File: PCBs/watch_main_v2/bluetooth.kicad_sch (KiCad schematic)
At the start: 24 parts, among them U301 NRF5340-QKAA-R7, Y301 32MHz

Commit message: Schematic v2 complete
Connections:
- net RST renamed SWD.RST
- net SWCLK renamed SWD.SWCLK
- net SWDIO renamed SWD.SWDIO
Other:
- moved on the sheet: C1922, L301, L302, L303, TP804, TP805, U301A, U301B, Y301

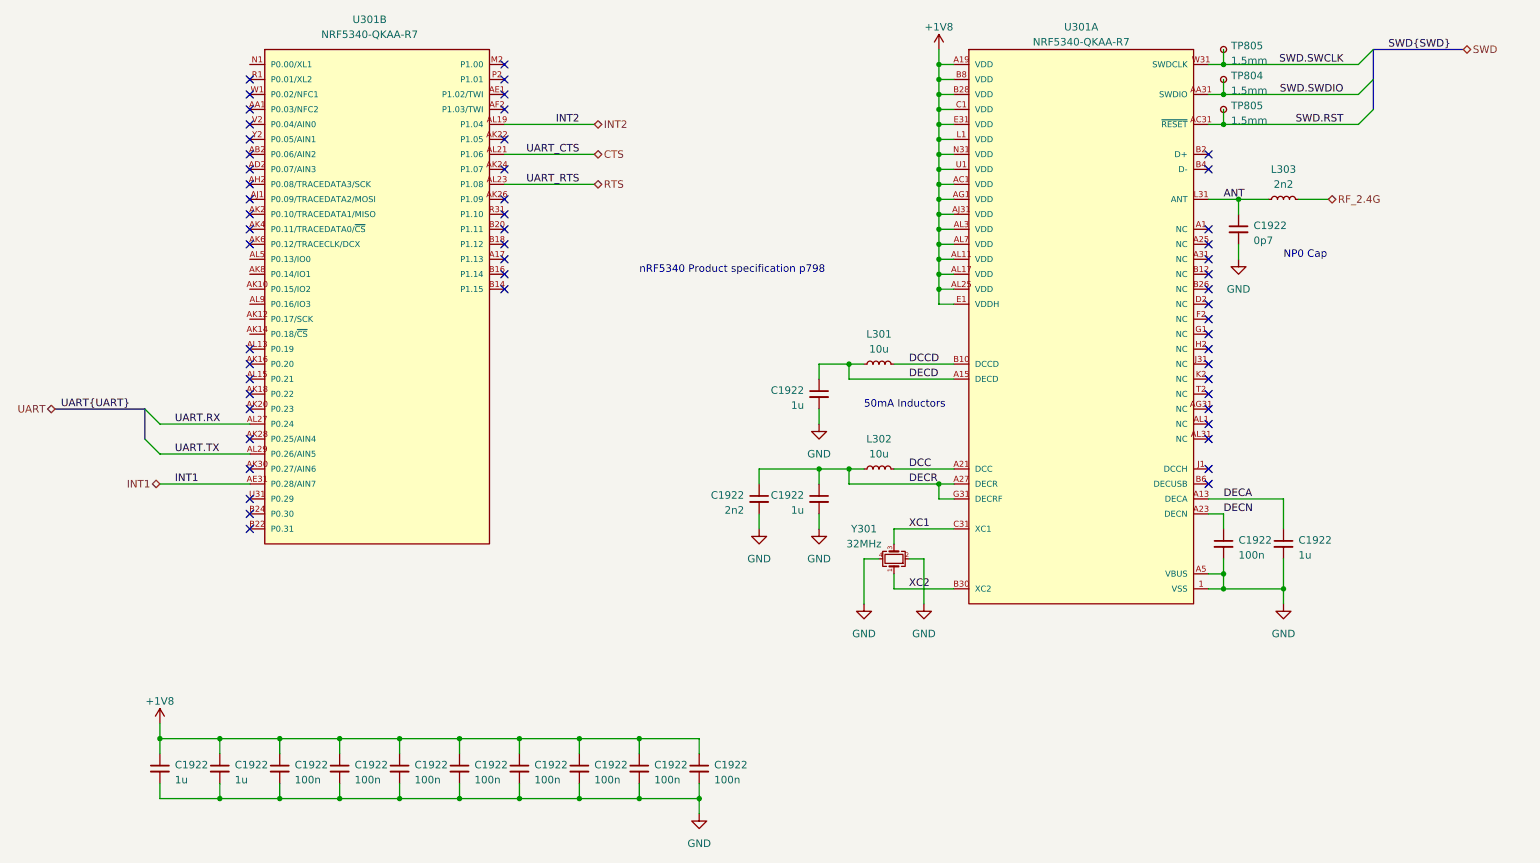
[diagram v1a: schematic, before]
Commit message: 262 Unrouted traces, fixed clearance issues
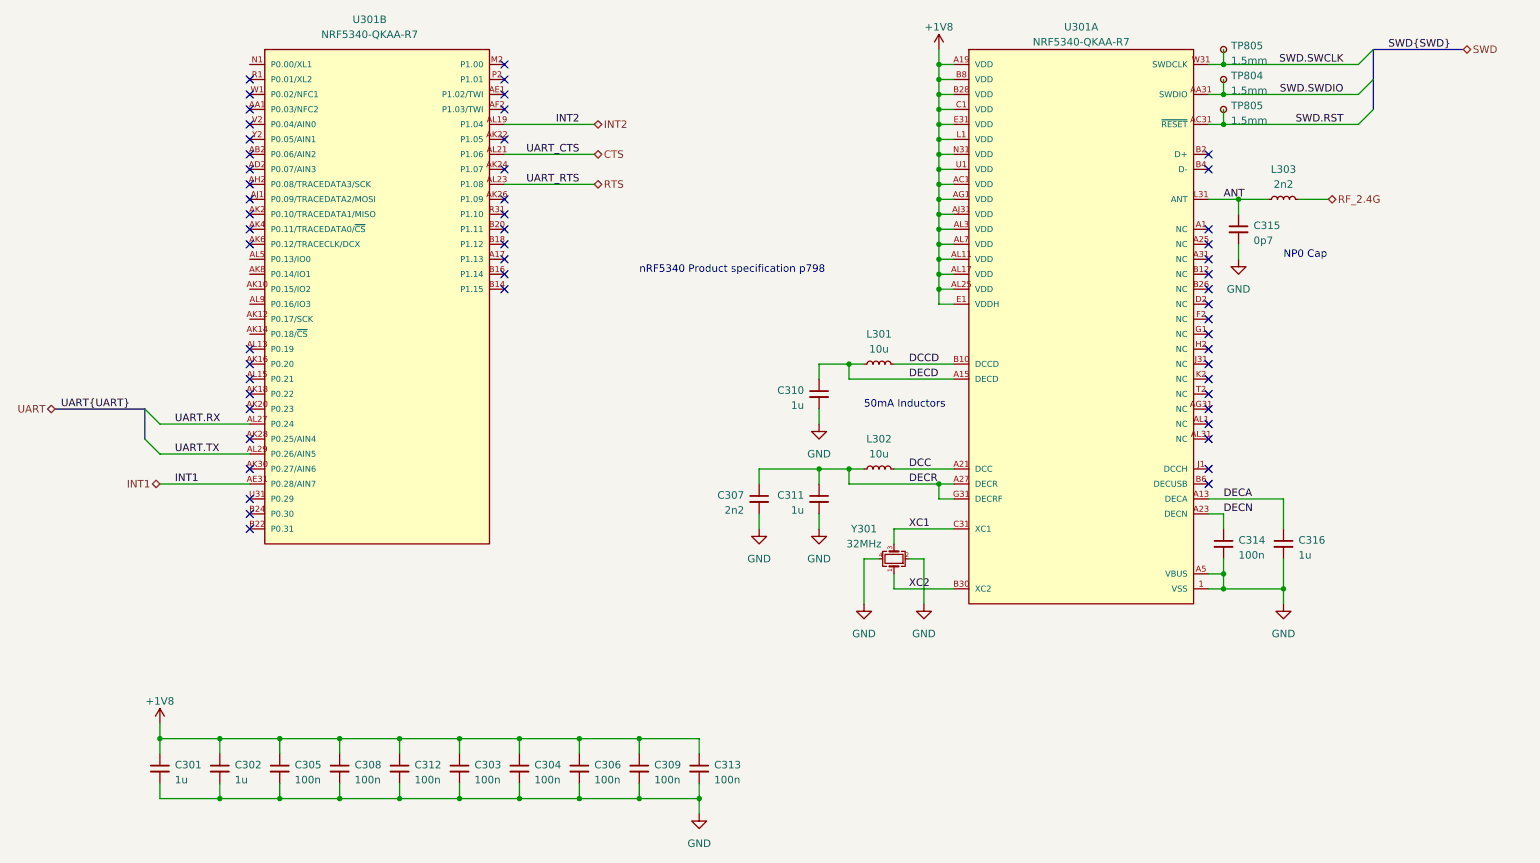
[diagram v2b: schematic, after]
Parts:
- renumbered C1922 to C301, C1922 to C302, C1922 to C303, C1922 to C304, C1922 to C305, C1922 to C306, C1922 to C307, C1922 to C308, C1922 to C309, C1922 to C310, C1922 to C311, C1922 to C312, C1922 to C313, C1922 to C314, C1922 to C315, C1922 to C316
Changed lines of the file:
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@@
   (symbol (lib_id "Device:C_Small") (at 228.6 73.66 0) (unit 1)
     (in_bom yes) (on_board yes) (dnp no)
-    (property "Reference" "C1922" (at 231.14 73.0313 0)
+    (property "Reference" "C315" (at 231.14 73.0313 0)
       (effects (font (size 1.27 1.27)) (justify left))
     )
@@
   (symbol (lib_id "Device:C_Small") (at 147.32 119.38 0) (mirror y) (unit 1)
     (in_bom yes) (on_board yes) (dnp no)
-    (property "Reference" "C1922" (at 144.78 118.7513 0)
+    (property "Reference" "C307" (at 144.78 118.7513 0)
       (effects (font (size 1.27 1.27)) (justify left))
     )
@@
   (symbol (lib_id "Device:C_Small") (at 127 165.1 0) (unit 1)
     (in_bom yes) (on_board yes) (dnp no)
-    (property "Reference" "C1922" (at 129.54 164.4713 0)
+    (property "Reference" "C309" (at 129.54 164.4713 0)
       (effects (font (size 1.27 1.27)) (justify left))
     )
@@
   (symbol (lib_id "Device:C_Small") (at 106.68 165.1 0) (unit 1)
     (in_bom yes) (on_board yes) (dnp no)
-    (property "Reference" "C1922" (at 109.22 164.4713 0)
+    (property "Reference" "C304" (at 109.22 164.4713 0)
       (effects (font (size 1.27 1.27)) (justify left))
     )
@@
   (symbol (lib_id "Device:C_Small") (at 45.72 165.1 0) (unit 1)
     (in_bom yes) (on_board yes) (dnp no)
-    (property "Reference" "C1922" (at 48.26 164.4713 0)
+    (property "Reference" "C301" (at 48.26 164.4713 0)
       (effects (font (size 1.27 1.27)) (justify left))
     )
@@
   (symbol (lib_id "Device:C_Small") (at 157.48 119.38 0) (mirror y) (unit 1)
     (in_bom yes) (on_board yes) (dnp no)
-    (property "Reference" "C1922" (at 154.94 118.7513 0)
+    (property "Reference" "C311" (at 154.94 118.7513 0)
       (effects (font (size 1.27 1.27)) (justify left))
     )
@@
   (symbol (lib_id "Device:C_Small") (at 116.84 165.1 0) (unit 1)
     (in_bom yes) (on_board yes) (dnp no)
-    (property "Reference" "C1922" (at 119.38 164.4713 0)
+    (property "Reference" "C306" (at 119.38 164.4713 0)
       (effects (font (size 1.27 1.27)) (justify left))
     )
@@
   (symbol (lib_id "Device:C_Small") (at 226.06 127 0) (unit 1)
     (in_bom yes) (on_board yes) (dnp no)
-    (property "Reference" "C1922" (at 228.6 126.3713 0)
+    (property "Reference" "C314" (at 228.6 126.3713 0)
       (effects (font (size 1.27 1.27)) (justify left))
     )
@@
   (symbol (lib_id "Device:C_Small") (at 55.88 165.1 0) (unit 1)
     (in_bom yes) (on_board yes) (dnp no)
-    (property "Reference" "C1922" (at 58.42 164.4713 0)
+    (property "Reference" "C302" (at 58.42 164.4713 0)
       (effects (font (size 1.27 1.27)) (justify left))
     )
@@
   (symbol (lib_id "Device:C_Small") (at 236.22 127 0) (unit 1)
     (in_bom yes) (on_board yes) (dnp no)
-    (property "Reference" "C1922" (at 238.76 126.3713 0)
+    (property "Reference" "C316" (at 238.76 126.3713 0)
       (effects (font (size 1.27 1.27)) (justify left))
     )
@@
   (symbol (lib_id "Device:C_Small") (at 137.16 165.1 0) (unit 1)
     (in_bom yes) (on_board yes) (dnp no)
-    (property "Reference" "C1922" (at 139.7 164.4713 0)
+    (property "Reference" "C313" (at 139.7 164.4713 0)
       (effects (font (size 1.27 1.27)) (justify left))
     )
@@
   (symbol (lib_id "Device:C_Small") (at 86.36 165.1 0) (unit 1)
     (in_bom yes) (on_board yes) (dnp no)
-    (property "Reference" "C1922" (at 88.9 164.4713 0)
+    (property "Reference" "C312" (at 88.9 164.4713 0)
       (effects (font (size 1.27 1.27)) (justify left))
     )
@@
   (symbol (lib_id "Device:C_Small") (at 76.2 165.1 0) (unit 1)
     (in_bom yes) (on_board yes) (dnp no)
-    (property "Reference" "C1922" (at 78.74 164.4713 0)
+    (property "Reference" "C308" (at 78.74 164.4713 0)
       (effects (font (size 1.27 1.27)) (justify left))
     )
@@
   (symbol (lib_id "Device:C_Small") (at 66.04 165.1 0) (unit 1)
     (in_bom yes) (on_board yes) (dnp no)
-    (property "Reference" "C1922" (at 68.58 164.4713 0)
+    (property "Reference" "C305" (at 68.58 164.4713 0)
       (effects (font (size 1.27 1.27)) (justify left))
     )
@@
   (symbol (lib_id "Device:C_Small") (at 157.48 101.6 0) (mirror y) (unit 1)
     (in_bom yes) (on_board yes) (dnp no)
-    (property "Reference" "C1922" (at 154.94 100.9713 0)
+    (property "Reference" "C310" (at 154.94 100.9713 0)
       (effects (font (size 1.27 1.27)) (justify left))
     )
@@
   (symbol (lib_id "Device:C_Small") (at 96.52 165.1 0) (unit 1)
     (in_bom yes) (on_board yes) (dnp no)
-    (property "Reference" "C1922" (at 99.06 164.4713 0)
-      (effects (font (size 1.27 1.27)) (justify left))
-    )
+    (property "Reference" "C303" (at 99.06 164.4713 0)
+      (effects (font (size 1.27 1.27)) (justify left))
+    )

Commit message: 190 Unrouted traces
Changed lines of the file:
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@@
-    )
-  )
-  (hierarchical_label "SWD" (shape bidirectional) (at 266.7 43.18 0) (fields_autoplaced)
-    (effects (font (size 1.27 1.27)) (justify left))
-    (property "DSI" "DSI" (at 233.68 44.45 0)
-      (effects (font (size 1.27 1.27) italic) (justify right) hide)
     )
   )

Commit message: Main board v2 complete
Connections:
- net CTS: now also U301.AL19 (P1.04); no longer U301.AL21 (P1.06)
- net INT1: now also U301.AL27 (P0.24); no longer U301.AE31 (P0.28/AIN7)
- net INT2: now also U301.AL23 (P1.08); no longer U301.AL19 (P1.04)
- net RTS: now also U301.AL21 (P1.06); no longer U301.AL23 (P1.08)
- net UART.RX: now also U301.AL29 (P0.26/AIN5); no longer U301.AL27 (P0.24)
- net UART.TX: now also U301.AE31 (P0.28/AIN7); no longer U301.AL29 (P0.26/AIN5)
- no-connect marks 54 -> 61
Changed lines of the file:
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@@
   (no_connect (at 60.96 60.96))
   (no_connect (at 104.14 78.74))
+  (no_connect (at 60.96 81.28))
   (no_connect (at 223.52 88.9))
   (no_connect (at 223.52 76.2))
   (no_connect (at 104.14 83.82))
   (no_connect (at 104.14 50.8))
+  (no_connect (at 60.96 78.74))
   (no_connect (at 104.14 73.66))
   (no_connect (at 60.96 63.5))
+  (no_connect (at 60.96 86.36))
   (no_connect (at 60.96 101.6))
   (no_connect (at 223.52 104.14))
@@
   (no_connect (at 223.52 83.82))
   (no_connect (at 223.52 91.44))
+  (no_connect (at 60.96 45.72))
   (no_connect (at 60.96 114.3))
   (no_connect (at 223.52 81.28))
   (no_connect (at 223.52 63.5))
+  (no_connect (at 60.96 91.44))
   (no_connect (at 60.96 104.14))
+  (no_connect (at 60.96 88.9))
   (no_connect (at 104.14 68.58))
   (no_connect (at 60.96 109.22))
@@
   (no_connect (at 104.14 48.26))
   (no_connect (at 104.14 81.28))
+  (no_connect (at 60.96 83.82))
   (no_connect (at 223.52 78.74))
   (no_connect (at 223.52 60.96))
@@
   (no_connect (at 60.96 73.66))
   (no_connect (at 223.52 99.06))
+  (bus_entry (at 43.18 109.22) (size 2.54 2.54)
+    (stroke (width 0) (type default))
+  )
   (bus_entry (at 251.46 48.26) (size -2.54 2.54)
     (stroke (width 0) (type default))
   )
-  (bus_entry (at 43.18 109.22) (size 2.54 2.54)
-    (stroke (width 0) (type default))
-  )
   (bus_entry (at 251.46 43.18) (size -2.54 2.54)
     (stroke (width 0) (type default))
   )
-  (bus_entry (at 43.18 104.14) (size 2.54 2.54)
-    (stroke (width 0) (type default))
-  )
-  (bus_entry (at 251.46 53.34) (size -2.54 2.54)
+  (bus_entry (at 43.18 114.3) (size 2.54 2.54)
     (stroke (width 0) (type default))
   )
@@
     (stroke (width 0) (type default))
   )
+  (bus (pts (xy 43.18 109.22) (xy 27.94 109.22))
+    (stroke (width 0) (type default))
+  )
   (wire (pts (xy 157.48 104.14) (xy 157.48 106.68))
     (stroke (width 0) (type default))
@@
     (stroke (width 0) (type default))
   )
-  (wire (pts (xy 45.72 106.68) (xy 60.96 106.68))
+  (wire (pts (xy 27.94 106.68) (xy 60.96 106.68))
     (stroke (width 0) (type default))
   )
@@
     (stroke (width 0) (type default))
   )
-  (bus (pts (xy 251.46 48.26) (xy 251.46 53.34))
-    (stroke (width 0) (type default))
-  )
   (wire (pts (xy 157.48 114.3) (xy 162.56 114.3))
     (stroke (width 0) (type default))
@@
     (stroke (width 0) (type default))
   )
-  (bus (pts (xy 43.18 104.14) (xy 43.18 109.22))
-    (stroke (width 0) (type default))
-  )
   (wire (pts (xy 104.14 55.88) (xy 119.38 55.88))
     (stroke (width 0) (type default))
@@
     (stroke (width 0) (type default))
   )
-  (wire (pts (xy 248.92 55.88) (xy 226.06 55.88))
-    (stroke (width 0) (type default))
-  )
   (wire (pts (xy 137.16 170.18) (xy 127 170.18))
     (stroke (width 0) (type default))
@@
     (stroke (width 0) (type default))
   )
+  (wire (pts (xy 226.06 55.88) (xy 246.38 55.88))
+    (stroke (width 0) (type default))
+  )
   (wire (pts (xy 226.06 124.46) (xy 226.06 121.92))
     (stroke (width 0) (type default))
@@
     (stroke (width 0) (type default))
   )
+  (bus (pts (xy 43.18 109.22) (xy 43.18 114.3))
+    (stroke (width 0) (type default))
+  )
   (wire (pts (xy 177.8 55.88) (xy 177.8 58.42))
     (stroke (width 0) (type default))
   )
-  (bus (pts (xy 43.18 104.14) (xy 27.94 104.14))
-    (stroke (width 0) (type default))
-  )
   (wire (pts (xy 116.84 160.02) (xy 116.84 162.56))
     (stroke (width 0) (type default))
@@
     (effects (font (size 1.27 1.27)) (justify left bottom))
   )
-  (label "UART{UART}" (at 40.64 104.14 180) (fields_autoplaced)
-    (effects (font (size 1.27 1.27)) (justify right bottom))
-  )
-  (label "INT2" (at 116.84 55.88 180) (fields_autoplaced)
+  (label "INT2" (at 116.84 66.04 180) (fields_autoplaced)
+    (effects (font (size 1.27 1.27)) (justify right bottom))
+  )
+  (label "UART{UART}" (at 40.64 109.22 180) (fields_autoplaced)
     (effects (font (size 1.27 1.27)) (justify right bottom))
   )
@@
     (effects (font (size 1.27 1.27)) (justify left bottom))
   )
-  (label "INT1" (at 48.26 116.84 0) (fields_autoplaced)
-    (effects (font (size 1.27 1.27)) (justify left bottom))
-  )
   (label "DECA" (at 226.06 119.38 0) (fields_autoplaced)
     (effects (font (size 1.27 1.27)) (justify left bottom))
@@
     (effects (font (size 1.27 1.27)) (justify left bottom))
   )
+  (label "INT1" (at 48.26 106.68 0) (fields_autoplaced)
+    (effects (font (size 1.27 1.27)) (justify left bottom))
+  )
   (label "DCC" (at 172.72 114.3 0) (fields_autoplaced)
     (effects (font (size 1.27 1.27)) (justify left bottom))
   )
-  (label "UART.RX" (at 48.26 106.68 0) (fields_autoplaced)
-    (effects (font (size 1.27 1.27)) (justify left bottom))
-  )
-  (label "UART_RTS" (at 116.84 66.04 180) (fields_autoplaced)
+  (label "UART.RX" (at 48.26 111.76 0) (fields_autoplaced)
+    (effects (font (size 1.27 1.27)) (justify left bottom))
+  )
+  (label "UART_RTS" (at 116.84 60.96 180) (fields_autoplaced)
     (effects (font (size 1.27 1.27)) (justify right bottom))
   )
@@
     (effects (font (size 1.27 1.27)) (justify left bottom))
   )
+  (label "UART.TX" (at 48.26 116.84 0) (fields_autoplaced)
+    (effects (font (size 1.27 1.27)) (justify left bottom))
+  )
   (label "XC2" (at 172.72 134.62 0) (fields_autoplaced)
     (effects (font (size 1.27 1.27)) (justify left bottom))
   )
-  (label "UART.TX" (at 48.26 111.76 0) (fields_autoplaced)
-    (effects (font (size 1.27 1.27)) (justify left bottom))
-  )
-  (label "UART_CTS" (at 116.84 60.96 180) (fields_autoplaced)
+  (label "UART_CTS" (at 116.84 55.88 180) (fields_autoplaced)
     (effects (font (size 1.27 1.27)) (justify right bottom))
   )
@@
     (effects (font (size 1.27 1.27)) (justify right bottom))
   )
-  (hierarchical_label "INT2" (shape bidirectional) (at 119.38 55.88 0) (fields_autoplaced)
+  (hierarchical_label "INT2" (shape bidirectional) (at 119.38 66.04 0) (fields_autoplaced)
     (effects (font (size 1.27 1.27)) (justify left))
   )
-  (hierarchical_label "CTS" (shape bidirectional) (at 119.38 60.96 0) (fields_autoplaced)
+  (hierarchical_label "CTS" (shape bidirectional) (at 119.38 55.88 0) (fields_autoplaced)
     (effects (font (size 1.27 1.27)) (justify left))
   )
-  (hierarchical_label "RTS" (shape bidirectional) (at 119.38 66.04 0) (fields_autoplaced)
+  (hierarchical_label "RTS" (shape bidirectional) (at 119.38 60.96 0) (fields_autoplaced)
     (effects (font (size 1.27 1.27)) (justify left))
+  )
+  (hierarchical_label "UART" (shape bidirectional) (at 27.94 109.22 180) (fields_autoplaced)
+    (effects (font (size 1.27 1.27)) (justify right))
+    (property "DSI" "DSI" (at 27.94 110.49 0)
+      (effects (font (size 1.27 1.27) italic) (justify right) hide)
+    )
   )
   (hierarchical_label "RF_2.4G" (shape bidirectional) (at 243.84 68.58 0) (fields_autoplaced)
     (effects (font (size 1.27 1.27)) (justify left))
   )
-  (hierarchical_label "INT1" (shape bidirectional) (at 45.72 116.84 180) (fields_autoplaced)
+  (hierarchical_label "INT1" (shape bidirectional) (at 27.94 106.68 180) (fields_autoplaced)
     (effects (font (size 1.27 1.27)) (justify right))
   )
-  (hierarchical_label "UART" (shape bidirectional) (at 27.94 104.14 180) (fields_autoplaced)
-    (effects (font (size 1.27 1.27)) (justify right))
-    (property "DSI" "DSI" (at 27.94 105.41 0)
-      (effects (font (size 1.27 1.27) italic) (justify right) hide)
-    )
-  )
   (netclass_flag "" (length 2.54) (shape round) (at 231.14 68.58 0) (fields_autoplaced)

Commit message: PCB V3 progress
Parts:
- renumbered TP805 to TP301, TP804 to TP302, TP805 to TP303
